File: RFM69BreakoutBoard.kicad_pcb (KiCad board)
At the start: 2 copper layers, 25.4 x 25.4 mm, 22 parts, among them P1 BB Holes, P10 TST, P11 TST, P12 TST, P13 TST, P2 TST, P3 TST, P4 TST, P5 TST, P6 TST, P7 TST, P8 TST, P9 TST, U1 MCP1703, U2 74HCT123, U3 RFM69HW

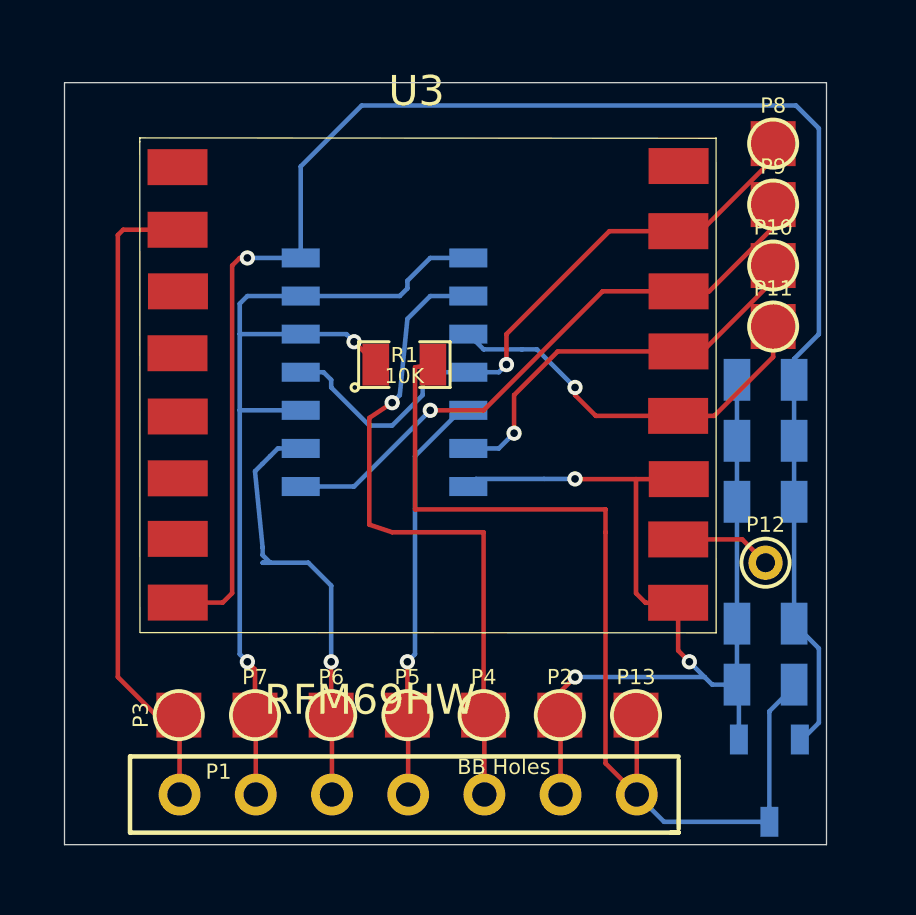
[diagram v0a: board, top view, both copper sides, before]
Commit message: 2nd pass at PCB layout
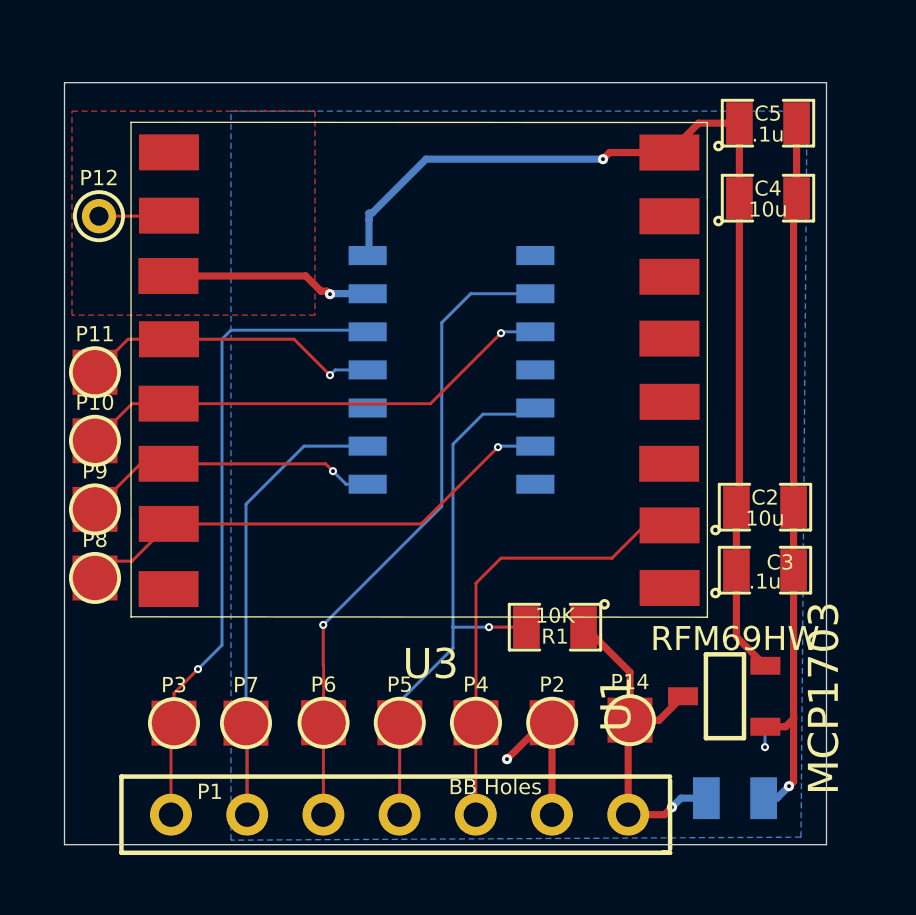
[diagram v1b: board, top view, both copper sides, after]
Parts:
- removed P13: TST, PINTST
- added P14: TST, PINTST, F.Cu at (76.0, 154.6)
- C2, C3, C4, C5, U1: moved to F.Cu
- moved P8 26.8 mm to (58.2, 149.9)
- moved P12 25.0 mm to (58.3, 137.8)
- moved P9 24.8 mm to (58.2, 147.6)
- moved P10 23.3 mm to (58.2, 145.3)
- moved P11 22.7 mm to (58.2, 143.0)
- moved R1 10.1 mm to (73.5, 151.5), turned to 180 degrees
- moved C5 8.56 mm to (80.6, 134.7), turned to 0 degrees
- moved C4 8.09 mm to (80.6, 137.2), turned to 0 degrees
- moved C1 3.92 mm to (79.5, 157.2), turned to 0 degrees
- moved U3 2.43 mm to (69.3, 142.0), turned to 180 degrees
- moved U2 2.23 mm to (70.0, 142.9)
- moved C3 1.78 mm to (80.5, 149.6), turned to 0 degrees
- moved U1 0.94 mm to (79.8, 155.2), turned to 90 degrees
- moved P1 0.73 mm to (67.0, 157.8)
- moved P7 0.40 mm to (63.2, 154.7)
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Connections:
- P1 pad 3: /CLK_5V -> /INT
- P1 pad 4: /MISO -> /CS_5V
- P1 pad 5: /MOSI_5V -> /MISO_5V
- P1 pad 6: /CS_5V -> /MOSI_5V
- P1 pad 7: /INT -> /CLK_5V
- P3 pad 1: /INT -> /CLK_5V
- P4 pad 1: /CLK_5V -> /INT
- P5 pad 1: /MISO -> /CS_5V
- P6 pad 1: /MOSI_5V -> /MISO_5V
- P7 pad 1: /CS_5V -> /MOSI_5V
- R1 pad 1: /CS_5V -> +5V
- R1 pad 2: +5V -> /CS_5V
- U2 pad 1: /CS_5V -> GND
- U2 pad 10: /CS_5V -> GND
- U2 pad 11: /CS_3V3 -> /CLK_3V3
- U2 pad 12: /CS_5V -> /CLK_5V
- U2 pad 13: /CS_5V -> GND
- U2 pad 2: /CLK_5V -> /MISO_5V
- U2 pad 3: /CLK_3V3 -> /MISO_3V3
- U2 pad 4: /CS_3V3 -> GND
- U2 pad 5: /MISO -> /CS_5V
- U2 pad 6: /MISO_3V3 -> /CS_3V3
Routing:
- net +3.3V: track 58.1 -> 33.6 mm
- net +5V: track 34.0 -> 11.9 mm, vias 0 -> 1
- net /MISO_5V: track 0.00 -> 21.6 mm, vias 0 -> 1
- net /MISO: track 13.8 -> 0.00 mm, vias 1 -> 0
- net /CS_5V: track 32.0 -> 21.8 mm, vias 2 -> 1
- net /MOSI_3V3: track 20.1 -> 10.0 mm
- net /INT: track 22.0 -> 15.0 mm
- net /CS_3V3: track 21.7 -> 16.5 mm
- net /MOSI_5V: track 14.8 -> 18.3 mm, vias 1 -> 0
- net /CLK_3V3: track 13.3 -> 10.1 mm
- net /MISO_3V3: track 13.7 -> 16.2 mm
- net /ANA: track 3.23 -> 2.34 mm
- net /CLK_5V: track 22.3 -> 21.6 mm
- net GND: track 37.0 -> 36.3 mm
- net (no net): track 0.00 -> 0.60 mm, vias 0 -> 1
- added copper zone on B.Cu, net GND
- added copper zone on F.Cu, net GND
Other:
- net class Default: trace_width 0.1524 -> 0.1; via_dia 0.508 -> 0.27; via_drill 0.3302 -> 0.13
- net class POWER added: clearance 0.1524, trace_width 0.24, via_dia 0.34, via_drill 0.2
- rule trace_min: 0.1524 -> 0.1
- rule via_min_drill: 0.3302 -> 0.13
- rule via_min_size: 0.508 -> 0.27

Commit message: moved C1 to front copper on layout board
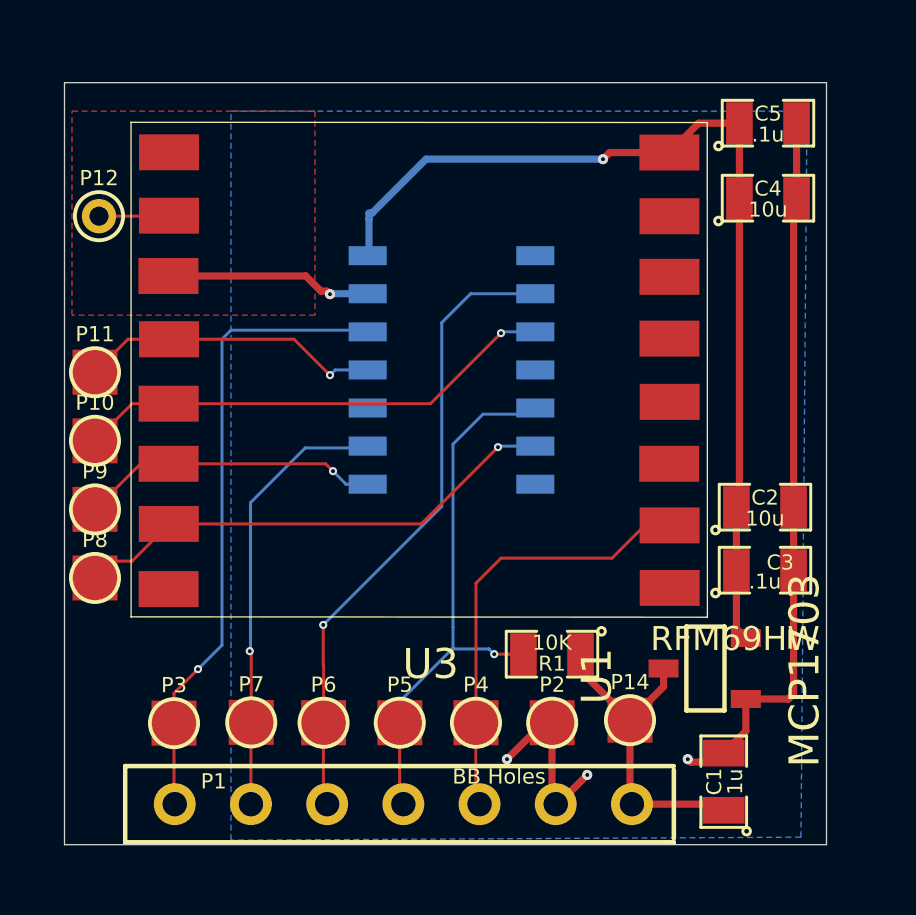
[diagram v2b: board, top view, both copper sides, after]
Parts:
- C1: moved to F.Cu
- moved U1 1.13 mm to (79.2, 154.3)
- moved R1 0.91 mm to (73.4, 152.4)
- moved C1 0.67 mm to (79.1, 156.7), turned to 90 degrees
- moved P1 0.37 mm to (67.2, 157.4)
- moved P7 0.18 mm to (63.4, 154.7)
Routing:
- net /MOSI_5V: track 18.3 -> 14.8 mm, vias 0 -> 1
- net GND: track 36.3 -> 37.6 mm, vias 3 -> 4
- net +3.3V: track 33.6 -> 32.4 mm
- net +5V: track 11.9 -> 11.0 mm, vias 1 -> 0
- net (no net): track 0.60 -> 0.00 mm, vias 1 -> 0

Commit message: added text to front and back silkscreen
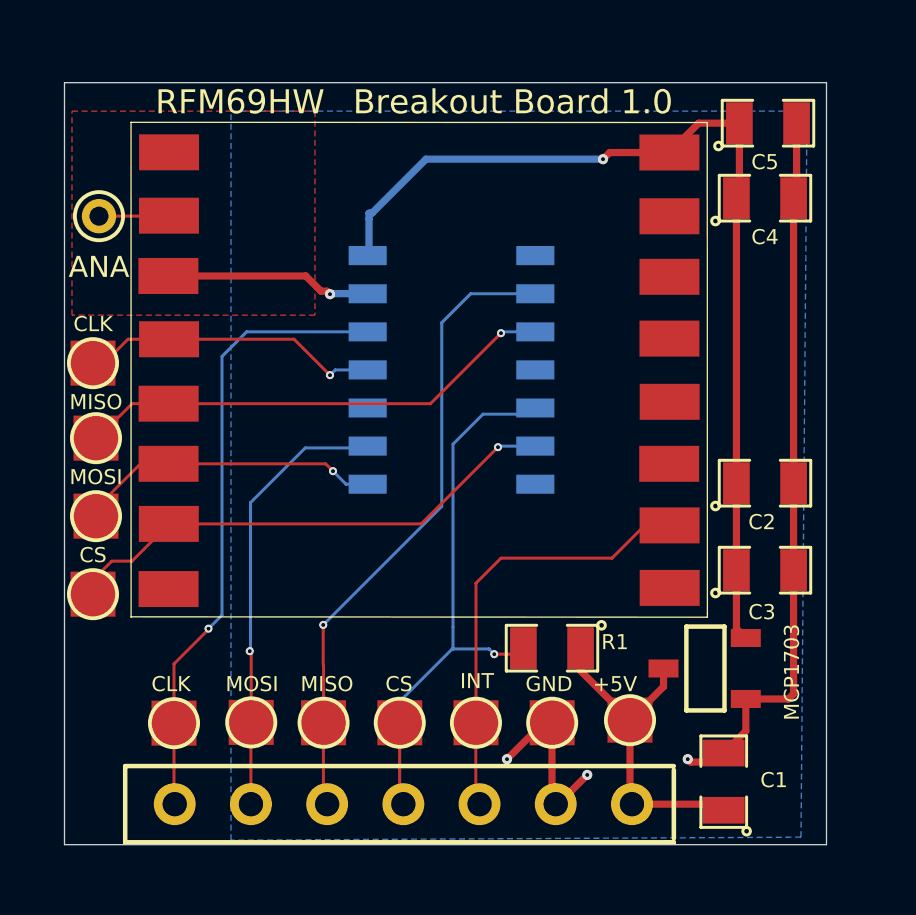
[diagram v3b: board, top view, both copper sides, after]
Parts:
- moved C2 0.80 mm to (80.5, 146.7)
- moved P8 0.54 mm to (58.1, 150.4)
- moved P11 0.31 mm to (58.1, 142.7)
- moved P9 0.23 mm to (58.2, 147.8)
- moved R1 0.20 mm to (73.4, 152.2)
- moved C4 0.10 mm to (80.5, 137.2)
- moved P10 0.09 mm to (58.2, 145.2)
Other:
- board text added: "+5V"
- board text added: "ANA"
- board text added: "Bitknitting.wordpress.com"
- board text added: "Breakout Board 1.0"
- board text added: "CLK"
- board text added: "CS"
- board text added: "GND"
- board text added: "INT"
- board text added: "MISO"
- board text added: "MOSI"
- board text added: "RFM69"
- board text added: "github.com/BitKnitting/ RFM69BreakoutBoard"

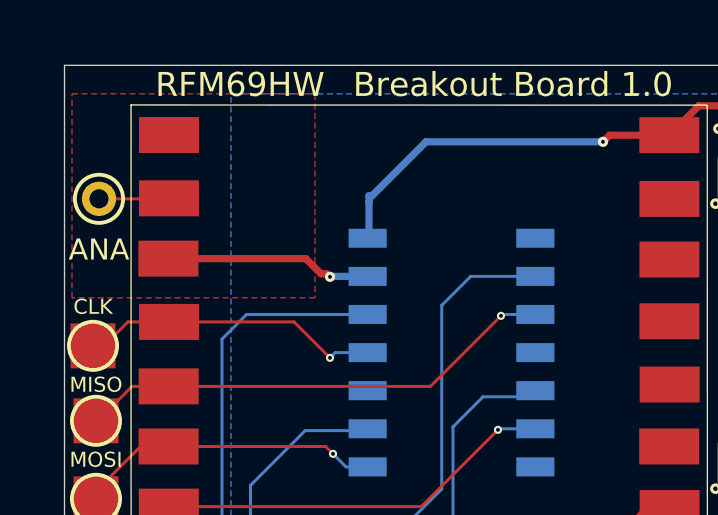
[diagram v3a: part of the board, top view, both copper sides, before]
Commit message: added via stitching to overlapping GND planes
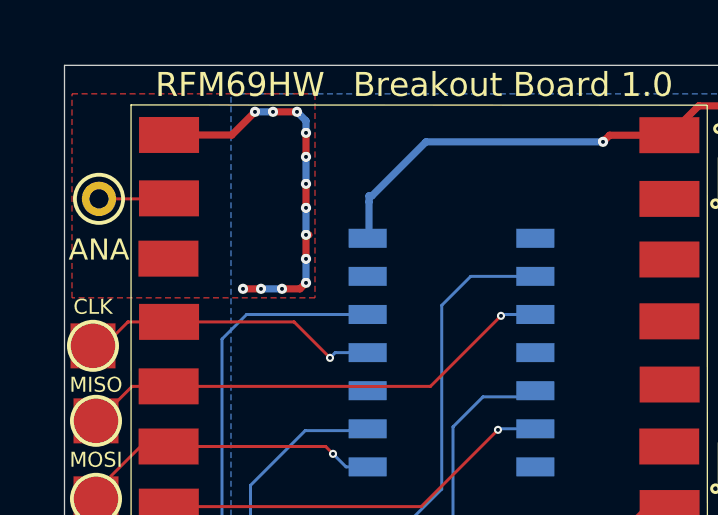
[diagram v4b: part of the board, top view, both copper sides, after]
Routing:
- net GND: track 37.5 -> 43.3 mm, vias 4 -> 16
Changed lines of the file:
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@@
     (links 44)
     (no_connects 0)
-    (area 56.952939 133.348749 82.840511 158.897401)
+    (area 56.886939 133.14 82.551251 158.897401)
     (thickness 1.6)
     (drawings 20)
-    (tracks 137)
+    (tracks 160)
     (zones 0)
     (modules 22)
@@
   (module RFM69HW (layer F.Cu)
     (at 69.342 141.986 180)
+    (zone_connect 1)
     (fp_text reference U3 (at -0.0127 -10.7442 180) (layer F.SilkS) hide
       (effects (font (size 1 1) (thickness 0.15)))
@@
     (pad 1 smd rect (at -7.98068 -8.20674 180) (size 2 1.2)
       (layers F.Cu F.Paste F.Mask)
+      (zone_connect 1)
     )
     (pad 2 smd rect (at -7.97814 -6.1214 180) (size 2 1.2)
       (layers F.Cu F.Paste F.Mask)
       (net 8 /INT)
+      (zone_connect 1)
     )
     (pad 3 smd rect (at -7.96544 -4.06908 180) (size 2 1.2)
       (layers F.Cu F.Paste F.Mask)
+      (zone_connect 1)
     )
     (pad 4 smd rect (at -7.98068 -2.00406 180) (size 2 1.2)
       (layers F.Cu F.Paste F.Mask)
+      (zone_connect 1)
     )
     (pad 5 smd rect (at -7.97306 0.10414 180) (size 2 1.2)
       (layers F.Cu F.Paste F.Mask)
+      (zone_connect 1)
     )
     (pad 6 smd rect (at -7.97306 2.16408 180) (size 2 1.2)
       (layers F.Cu F.Paste F.Mask)
+      (zone_connect 1)
     )
     (pad 7 smd rect (at -7.97306 4.18338 180) (size 2 1.2)
       (layers F.Cu F.Paste F.Mask)
+      (zone_connect 1)
     )
     (pad 8 smd rect (at -7.97052 6.30682 180) (size 2 1.2)
       (layers F.Cu F.Paste F.Mask)
       (net 1 +3.3V)
+      (zone_connect 1)
     )
     (pad 9 smd rect (at 8.70712 6.31444 180) (size 2 1.2)
       (layers F.Cu F.Paste F.Mask)
       (net 13 GND)
+      (zone_connect 1)
     )
     (pad 10 smd rect (at 8.70966 4.20116 180) (size 2 1.2)
       (layers F.Cu F.Paste F.Mask)
       (net 3 /ANA)
+      (zone_connect 1)
     )
     (pad 11 smd rect (at 8.72744 2.19202 180) (size 2 1.2)
       (layers F.Cu F.Paste F.Mask)
       (net 13 GND)
+      (zone_connect 1)
     )
     (pad 12 smd rect (at 8.70712 0.08382 180) (size 2 1.2)
       (layers F.Cu F.Paste F.Mask)
       (net 4 /CLK_3V3)
+      (zone_connect 1)
     )
     (pad 13 smd rect (at 8.71982 -2.06502 180) (size 2 1.2)
       (layers F.Cu F.Paste F.Mask)
       (net 9 /MISO_3V3)
+      (zone_connect 1)
     )
     (pad 14 smd rect (at 8.72236 -4.06908 180) (size 2 1.2)
       (layers F.Cu F.Paste F.Mask)
       (net 11 /MOSI_3V3)
+      (zone_connect 1)
     )
     (pad 15 smd rect (at 8.71474 -6.07314 180) (size 2 1.2)
       (layers F.Cu F.Paste F.Mask)
       (net 6 /CS_3V3)
+      (zone_connect 1)
     )
     (pad 16 smd rect (at 8.72236 -8.24484 180) (size 2 1.2)
       (layers F.Cu F.Paste F.Mask)
+      (zone_connect 1)
     )
   )
@@
   (segment (start 63.365 157.4) (end 63.365 154.685) (width 0.1) (layer F.Cu) (net 12))
   (segment (start 63.365 154.685) (end 63.375 154.675) (width 0.1) (layer F.Cu) (net 12))
+  (segment (start 65.2 139) (end 65.2 139.8) (width 0.24) (layer F.Cu) (net 13))
+  (via (at 63.1 140.8) (size 0.34) (layers F.Cu B.Cu) (net 13))
+  (segment (start 63.7 140.8) (end 63.1 140.8) (width 0.24) (layer F.Cu) (net 13))
+  (via (at 63.7 140.8) (size 0.34) (layers F.Cu B.Cu) (net 13))
+  (segment (start 64.4 140.8) (end 63.7 140.8) (width 0.24) (layer B.Cu) (net 13))
+  (via (at 64.4 140.8) (size 0.34) (layers F.Cu B.Cu) (net 13))
+  (segment (start 65 140.8) (end 64.4 140.8) (width 0.24) (layer F.Cu) (net 13))
+  (segment (start 65.2 140.6) (end 65 140.8) (width 0.24) (layer F.Cu) (net 13))
+  (via (at 65.2 140.6) (size 0.34) (layers F.Cu B.Cu) (net 13))
+  (segment (start 65.2 139.8) (end 65.2 140.6) (width 0.24) (layer B.Cu) (net 13))
+  (via (at 65.2 139.8) (size 0.34) (layers F.Cu B.Cu) (net 13))
+  (segment (start 60.63488 135.67156) (end 62.72844 135.67156) (width 0.24) (layer F.Cu) (net 13) (status 400000))
+  (segment (start 65.2 139) (end 65.3 139) (width 0.24) (layer F.Cu) (net 13))
+  (via (at 65.2 139) (size 0.34) (layers F.Cu B.Cu) (net 13))
+  (segment (start 65.2 138.1) (end 65.2 139) (width 0.24) (layer B.Cu) (net 13))
+  (via (at 65.2 138.1) (size 0.34) (layers F.Cu B.Cu) (net 13))
+  (segment (start 65.2 137.3) (end 65.2 138.1) (width 0.24) (layer F.Cu) (net 13))
+  (via (at 65.2 137.3) (size 0.34) (layers F.Cu B.Cu) (net 13))
+  (segment (start 65.2 136.4) (end 65.2 137.3) (width 0.24) (layer B.Cu) (net 13))
+  (via (at 65.2 136.4) (size 0.34) (layers F.Cu B.Cu) (net 13))
+  (segment (start 65.2 135.6) (end 65.2 136.4) (width 0.24) (layer F.Cu) (net 13))
+  (via (at 65.2 135.6) (size 0.34) (layers F.Cu B.Cu) (net 13))
+  (segment (start 65.2 135.2) (end 65.2 135.6) (width 0.24) (layer B.Cu) (net 13))
+  (segment (start 64.9 134.9) (end 65.2 135.2) (width 0.24) (layer B.Cu) (net 13))
+  (via (at 64.9 134.9) (size 0.34) (layers F.Cu B.Cu) (net 13))
+  (segment (start 64.1 134.9) (end 64.9 134.9) (width 0.24) (layer F.Cu) (net 13))
+  (via (at 64.1 134.9) (size 0.34) (layers F.Cu B.Cu) (net 13))
+  (segment (start 63.5 134.9) (end 64.1 134.9) (width 0.24) (layer B.Cu) (net 13))
+  (via (at 63.5 134.9) (size 0.34) (layers F.Cu B.Cu) (net 13))
+  (segment (start 62.72844 135.67156) (end 63.5 134.9) (width 0.24) (layer F.Cu) (net 13))
   (segment (start 81.4525 146.7) (end 81.4525 137.2) (width 0.24) (layer F.Cu) (net 13))
   (segment (start 81.4525 149.6) (end 81.4525 146.7) (width 0.24) (layer F.Cu) (net 13))
@@
   (segment (start 73.4 154.692) (end 73.406 154.686) (width 0.24) (layer F.Cu) (net 13))
   (segment (start 81.5525 137.2) (end 81.5525 134.7) (width 0.24) (layer F.Cu) (net 13))
-  (segment (start 60.61456 139.79398) (end 65.19398 139.79398) (width 0.24) (layer F.Cu) (net 13))
-  (segment (start 66.015 140.385) (end 67.256 140.385) (width 0.24) (layer B.Cu) (net 13))
-  (segment (start 66 140.4) (end 66.015 140.385) (width 0.24) (layer B.Cu) (net 13))
-  (via (at 66 140.4) (size 0.34) (layers F.Cu B.Cu) (net 13))
-  (segment (start 65.9 140.3) (end 66 140.4) (width 0.24) (layer F.Cu) (net 13))
-  (segment (start 65.7 140.3) (end 65.9 140.3) (width 0.24) (layer F.Cu) (net 13))
-  (segment (start 65.19398 139.79398) (end 65.7 140.3) (width 0.24) (layer F.Cu) (net 13))
   (zone (net 13) (net_name GND) (layer B.Cu) (hatch edge 0.508)
     (connect_pads yes (clearance 0.508))

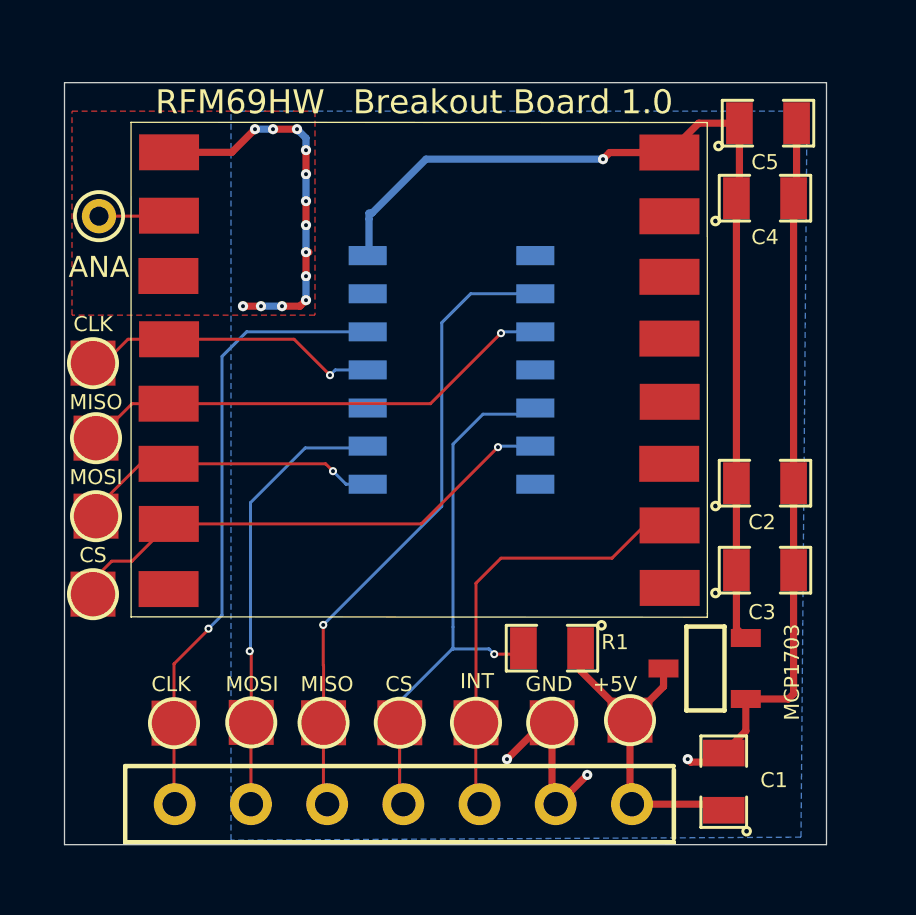
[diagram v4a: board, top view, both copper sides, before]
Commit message: adjusted space and spoke width around thermal relief pads in the GND plane
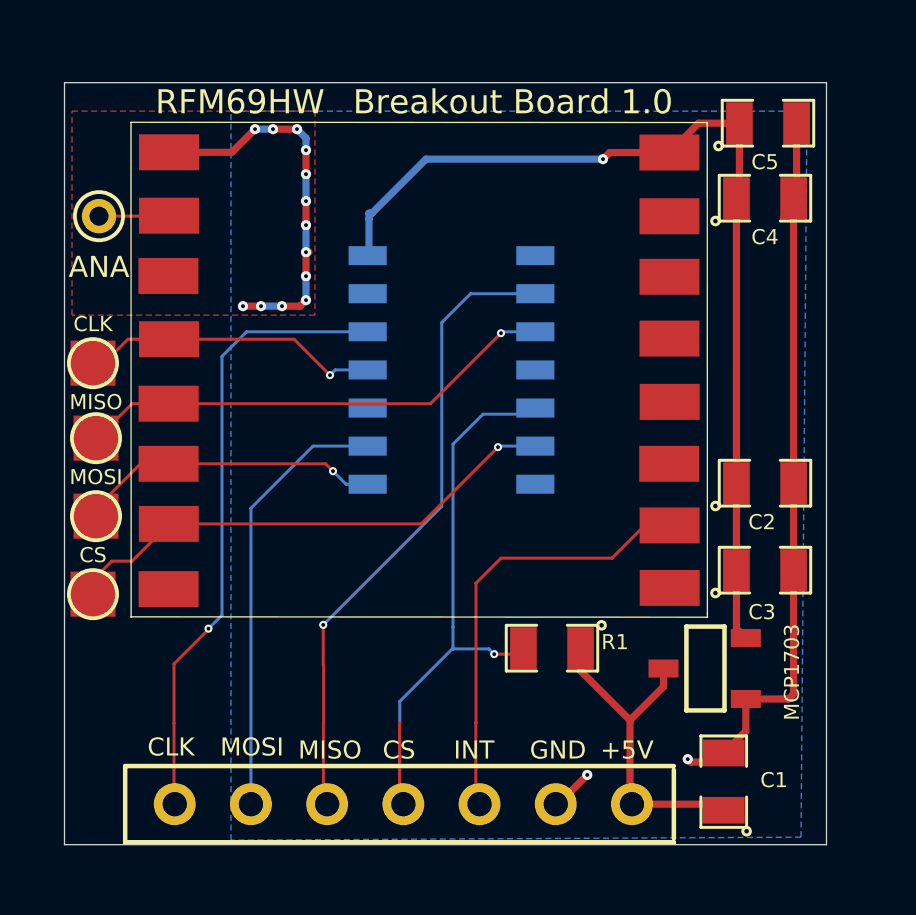
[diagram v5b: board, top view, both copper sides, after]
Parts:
- removed P14, P2, P3, P4, P5, P6, P7: TST, PINTST
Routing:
- net GND: track 43.3 -> 38.3 mm, vias 16 -> 15
- net /MOSI_5V: track 14.8 -> 14.6 mm, vias 1 -> 0
